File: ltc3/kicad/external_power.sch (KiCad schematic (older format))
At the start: 40 parts, among them IC701 TLP3542, IC702 TLP3542, IC703 TLP3542, IC704 TLP3542, M701 W28-XQ1A-1, M702 W28-XQ1A-1, M703 W28-XQ1A-1, M704 W28-XQ1A-1, P701 CONN_01X10, P702 CONN_01X10, P703 CONN_EXT_PWR_1, P704 CONN_EXT_PWR_2, P705 CONN_01X08, P706 CONN_01X08, P707 CONN_EXT_PWR_3, P708 CONN_EXT_PWR_4, Q701 PMV45EN, Q702 PMV45EN, Q703 PMV45EN, Q704 PMV45EN, SW701 SP3T, SW702 SP3T, SW703 SP3T, SW704 SP3T

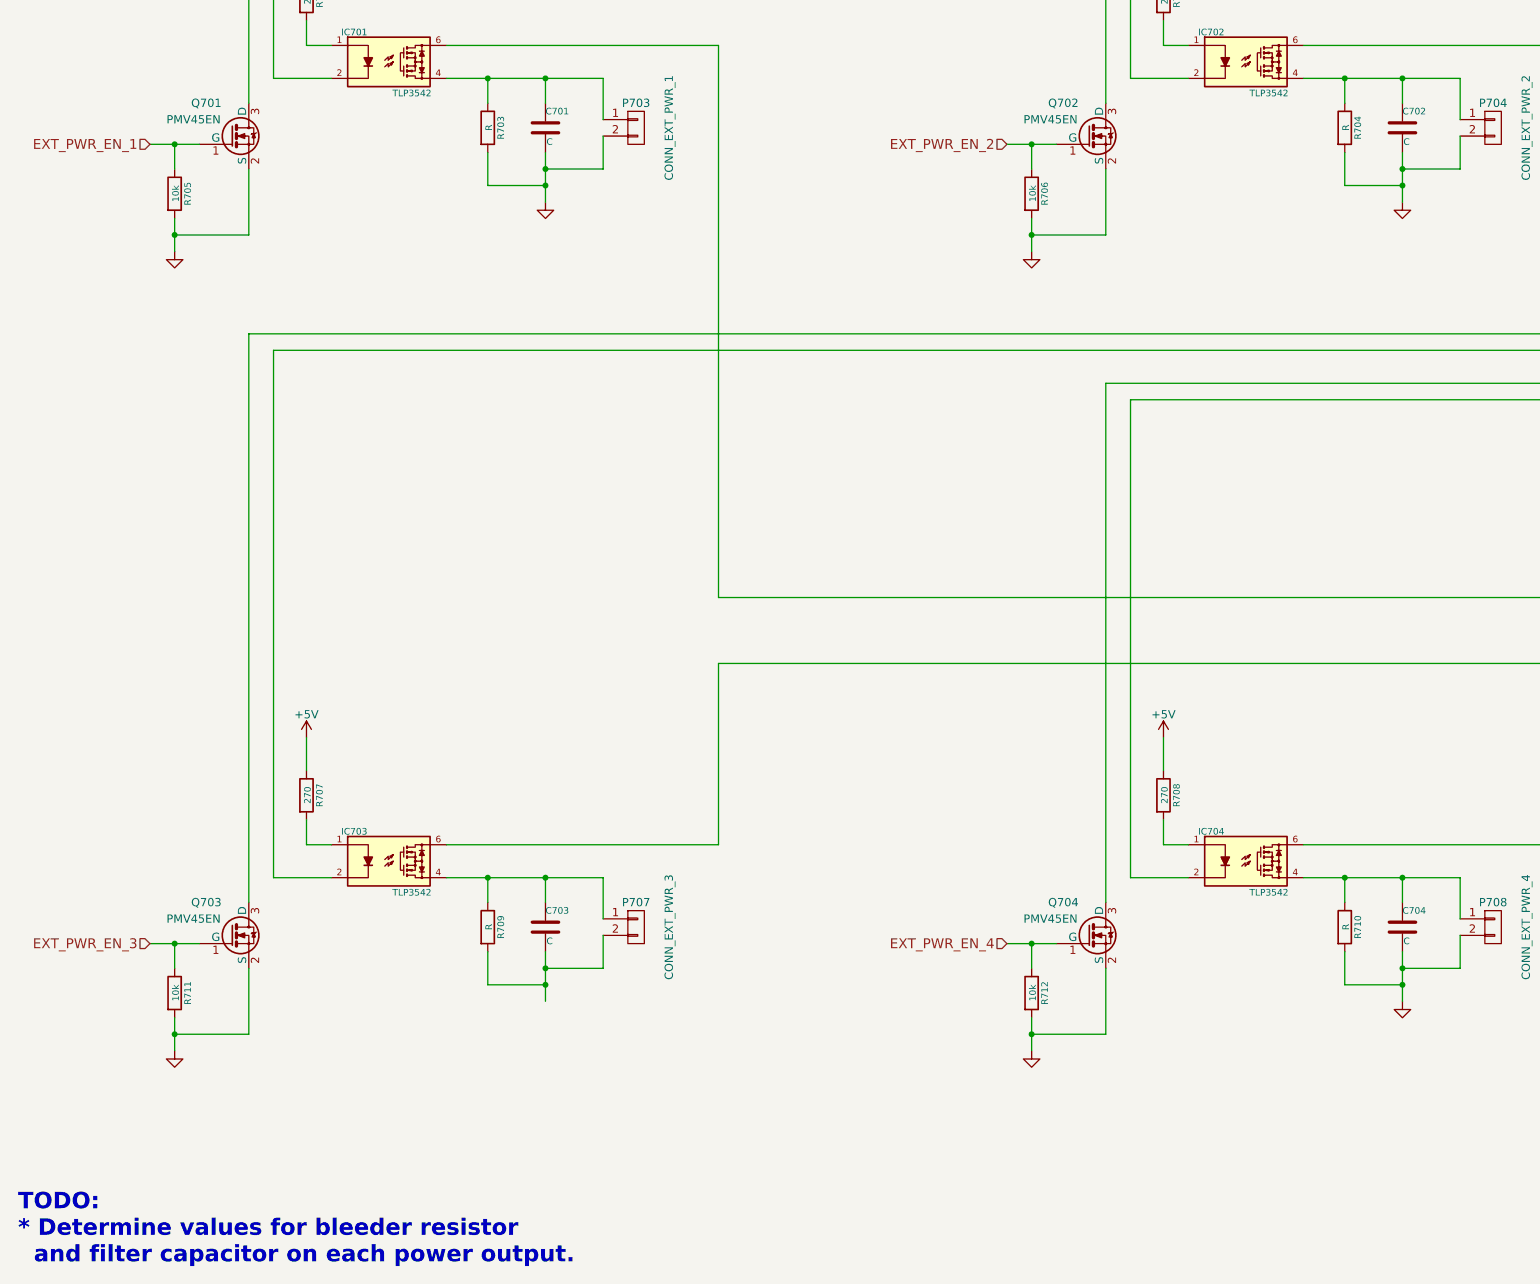
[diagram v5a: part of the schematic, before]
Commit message: LTC3: More component values and footprint assignments.
Split the two-in-one Beagle Bone expansion header component into two
separate components.  Otherwise, we'd be stuck with having to use a
single footprint for the BB cape pin headers, which means pin
numbering that doesn't match the BB docs.
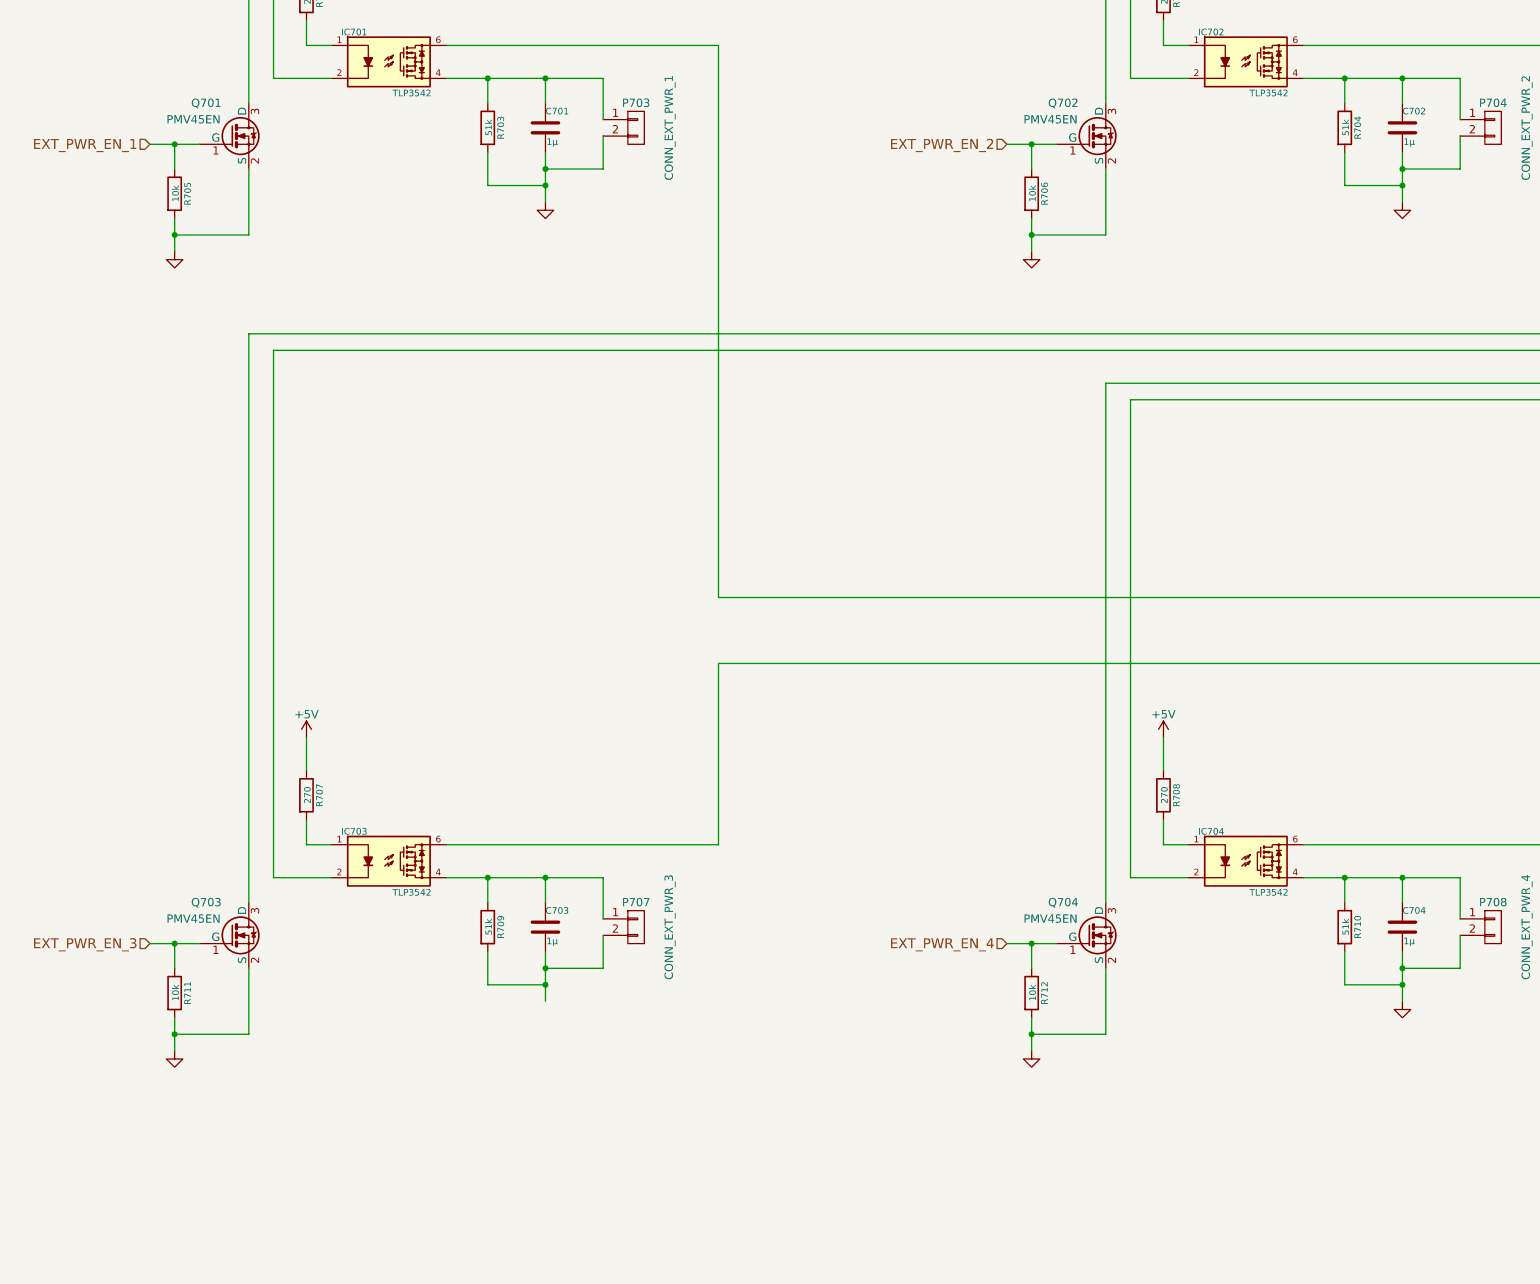
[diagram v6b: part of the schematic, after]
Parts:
- C701, C702, C703, C704: value C -> 1μ
- R703, R704, R709, R710: value R -> 51k
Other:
- note removed: "TODO:\n* Determine values for bleeder resistor\n and filter capacitor on each power output."
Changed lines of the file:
@@
 EESchema Schematic File Version 2
+LIBS:Launch_Tower_Computer_III-rescue
 LIBS:BeagleBone_Black
 LIBS:LT8490
@@
 LIBS:battery_single_cell
 LIBS:breakers
-LIBS:Launch_Tower_Computer_III-cache
 EELAYER 25 0
 EELAYER END
@@
 Comment4 ""
 $EndDescr
-Text Notes 700  10250 0    100  ~ 20
-TODO:\n* Determine values for bleeder resistor\n  and filter capacitor on each power output.
 $Comp
 L R R705
@@
 EXT_PWR_EN_1
 $Comp
-L GND #PWR0160
+L GND #PWR0161
 U 1 1 557E02AD
 P 1650 4100
-F 0 "#PWR0160" H 1650 4100 30  0001 C CNN
+F 0 "#PWR0161" H 1650 4100 30  0001 C CNN
 F 1 "GND" H 1650 4030 30  0001 C CNN
 F 2 "" H 1650 4100 60  0000 C CNN
@@
 P 3550 3350
 F 0 "R703" V 3630 3350 40  0000 C CNN
-F 1 "R" V 3557 3351 40  0000 C CNN
+F 1 "51k" V 3557 3351 40  0000 C CNN
 F 2 "" V 3480 3350 30  0001 C CNN
 F 3 "~" H 3550 3350 30  0000 C CNN
@@
 P 3900 3350
 F 0 "C701" H 3900 3450 40  0000 L CNN
-F 1 "C" H 3906 3265 40  0000 L CNN
+F 1 "1μ" H 3906 3265 40  0000 L CNN
 F 2 "" H 3938 3200 30  0001 C CNN
 F 3 "~" H 3900 3350 60  0000 C CNN
@@
 $EndComp
 $Comp
-L GND #PWR0161
+L GND #PWR0162
 U 1 1 557E02DD
 P 3900 3800
-F 0 "#PWR0161" H 3900 3800 30  0001 C CNN
+F 0 "#PWR0162" H 3900 3800 30  0001 C CNN
 F 1 "GND" H 3900 3730 30  0001 C CNN
 F 2 "" H 3900 3800 60  0000 C CNN
@@
 $EndComp
 $Comp
-L +5V #PWR0162
+L +5V #PWR0163
 U 1 1 56544A2B
 P 2450 2200
-F 0 "#PWR0162" H 2450 2050 50  0001 C CNN
+F 0 "#PWR0163" H 2450 2050 50  0001 C CNN
 F 1 "+5V" H 2450 2340 50  0000 C CNN
 F 2 "" H 2450 2200 60  0000 C CNN
@@
 EXT_PWR_EN_2
 $Comp
-L GND #PWR0163
+L GND #PWR0164
 U 1 1 56CA75BB
 P 6850 4100
-F 0 "#PWR0163" H 6850 4100 30  0001 C CNN
+F 0 "#PWR0164" H 6850 4100 30  0001 C CNN
 F 1 "GND" H 6850 4030 30  0001 C CNN
 F 2 "" H 6850 4100 60  0000 C CNN
@@
 P 8750 3350
 F 0 "R704" V 8830 3350 40  0000 C CNN
-F 1 "R" V 8757 3351 40  0000 C CNN
+F 1 "51k" V 8757 3351 40  0000 C CNN
 F 2 "" V 8680 3350 30  0001 C CNN
 F 3 "~" H 8750 3350 30  0000 C CNN
@@
 P 9100 3350
 F 0 "C702" H 9100 3450 40  0000 L CNN
-F 1 "C" H 9106 3265 40  0000 L CNN
+F 1 "1μ" H 9106 3265 40  0000 L CNN
 F 2 "Capacitors_SMD:C_0805" H 9138 3200 30  0001 C CNN
 F 3 "~" H 9100 3350 60  0000 C CNN
@@
 $EndComp
 $Comp
-L GND #PWR0164
+L GND #PWR0165
 U 1 1 56CA75CD
 P 9100 3800
-F 0 "#PWR0164" H 9100 3800 30  0001 C CNN
+F 0 "#PWR0165" H 9100 3800 30  0001 C CNN
 F 1 "GND" H 9100 3730 30  0001 C CNN
 F 2 "" H 9100 3800 60  0000 C CNN
@@
 $EndComp
 $Comp
-L +5V #PWR0165
+L +5V #PWR0166
 U 1 1 56CA760C
 P 7650 2200
-F 0 "#PWR0165" H 7650 2050 50  0001 C CNN
+F 0 "#PWR0166" H 7650 2050 50  0001 C CNN
 F 1 "+5V" H 7650 2340 50  0000 C CNN
 F 2 "" H 7650 2200 60  0000 C CNN
@@
 $EndComp
 $Comp
-L +12V #PWR0166
+L +12V #PWR0167
 U 1 1 56CA7612
 P 11800 5650
-F 0 "#PWR0166" H 11800 5500 50  0001 C CNN
+F 0 "#PWR0167" H 11800 5500 50  0001 C CNN
 F 1 "+12V" H 11800 5790 50  0000 C CNN
 F 2 "" H 11800 5650 60  0000 C CNN
@@
 EXT_PWR_EN_3
 $Comp
-L GND #PWR0167
+L GND #PWR0168
 U 1 1 56CA9336
 P 1650 8950
-F 0 "#PWR0167" H 1650 8950 30  0001 C CNN
+F 0 "#PWR0168" H 1650 8950 30  0001 C CNN
 F 1 "GND" H 1650 8880 30  0001 C CNN
 F 2 "" H 1650 8950 60  0000 C CNN
@@
 P 3550 8200
 F 0 "R709" V 3630 8200 40  0000 C CNN
-F 1 "R" V 3557 8201 40  0000 C CNN
+F 1 "51k" V 3557 8201 40  0000 C CNN
 F 2 "" V 3480 8200 30  0001 C CNN
 F 3 "~" H 3550 8200 30  0000 C CNN
@@
 P 3900 8200
 F 0 "C703" H 3900 8300 40  0000 L CNN
-F 1 "C" H 3906 8115 40  0000 L CNN
+F 1 "1μ" H 3906 8115 40  0000 L CNN
 F 2 "Capacitors_SMD:C_0805" H 3938 8050 30  0001 C CNN
 F 3 "~" H 3900 8200 60  0000 C CNN
@@
 $EndComp
 $Comp
-L +5V #PWR0168
+L +5V #PWR0169
 U 1 1 56CA9387
 P 2450 7050
-F 0 "#PWR0168" H 2450 6900 50  0001 C CNN
+F 0 "#PWR0169" H 2450 6900 50  0001 C CNN
 F 1 "+5V" H 2450 7190 50  0000 C CNN
 F 2 "" H 2450 7050 60  0000 C CNN
@@
 EXT_PWR_EN_4
 $Comp
-L GND #PWR0169
+L GND #PWR0170
 U 1 1 56CA93AD
 P 6850 8950
-F 0 "#PWR0169" H 6850 8950 30  0001 C CNN
+F 0 "#PWR0170" H 6850 8950 30  0001 C CNN
 F 1 "GND" H 6850 8880 30  0001 C CNN
 F 2 "" H 6850 8950 60  0000 C CNN
@@
 P 8750 8200
 F 0 "R710" V 8830 8200 40  0000 C CNN
-F 1 "R" V 8757 8201 40  0000 C CNN
+F 1 "51k" V 8757 8201 40  0000 C CNN
 F 2 "" V 8680 8200 30  0001 C CNN
 F 3 "~" H 8750 8200 30  0000 C CNN
@@
 P 9100 8200
 F 0 "C704" H 9100 8300 40  0000 L CNN
-F 1 "C" H 9106 8115 40  0000 L CNN
+F 1 "1μ" H 9106 8115 40  0000 L CNN
 F 2 "Capacitors_SMD:C_0805" H 9138 8050 30  0001 C CNN
 F 3 "~" H 9100 8200 60  0000 C CNN
@@
 $EndComp
 $Comp
-L GND #PWR0170
+L GND #PWR0171
 U 1 1 56CA93BF
 P 9100 8650
-F 0 "#PWR0170" H 9100 8650 30  0001 C CNN
+F 0 "#PWR0171" H 9100 8650 30  0001 C CNN
 F 1 "GND" H 9100 8580 30  0001 C CNN
 F 2 "" H 9100 8650 60  0000 C CNN
@@
 $EndComp
 $Comp
-L +5V #PWR0171
+L +5V #PWR0172
 U 1 1 56CA93FE
 P 7650 7050
-F 0 "#PWR0171" H 7650 6900 50  0001 C CNN
+F 0 "#PWR0172" H 7650 6900 50  0001 C CNN
 F 1 "+5V" H 7650 7190 50  0000 C CNN
 F 2 "" H 7650 7050 60  0000 C CNN
@@
 Manual Override Switches, Front Panel
 $Comp
-L GND #PWR0172
+L GND #PWR0173
 U 1 1 56DB5084
 P 11800 2800
-F 0 "#PWR0172" H 11800 2550 50  0001 C CNN
+F 0 "#PWR0173" H 11800 2550 50  0001 C CNN
 F 1 "GND" H 11808 2626 50  0001 C CNN
 F 2 "" H 11800 2800 50  0000 C CNN

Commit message: Assigned component footprints.
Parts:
- C701: footprint (none) -> Capacitors_SMD:C_0805
- R703, R704, R709, R710: footprint (none) -> Resistors_SMD:R_0805
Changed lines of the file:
@@
 EESchema Schematic File Version 2
-LIBS:Launch_Tower_Computer_III-rescue
 LIBS:BeagleBone_Black
 LIBS:LT8490
@@
 LIBS:battery_single_cell
 LIBS:breakers
+LIBS:Launch_Tower_Computer_III-cache
 EELAYER 25 0
 EELAYER END
@@
 F 0 "R703" V 3630 3350 40  0000 C CNN
 F 1 "51k" V 3557 3351 40  0000 C CNN
-F 2 "" V 3480 3350 30  0001 C CNN
+F 2 "Resistors_SMD:R_0805" V 3480 3350 30  0001 C CNN
 F 3 "~" H 3550 3350 30  0000 C CNN
 	1    3550 3350
@@
 F 0 "C701" H 3900 3450 40  0000 L CNN
 F 1 "1μ" H 3906 3265 40  0000 L CNN
-F 2 "" H 3938 3200 30  0001 C CNN
+F 2 "Capacitors_SMD:C_0805" H 3938 3200 30  0001 C CNN
 F 3 "~" H 3900 3350 60  0000 C CNN
 	1    3900 3350
@@
 F 0 "R704" V 8830 3350 40  0000 C CNN
 F 1 "51k" V 8757 3351 40  0000 C CNN
-F 2 "" V 8680 3350 30  0001 C CNN
+F 2 "Resistors_SMD:R_0805" V 8680 3350 30  0001 C CNN
 F 3 "~" H 8750 3350 30  0000 C CNN
 	1    8750 3350
@@
 F 0 "R709" V 3630 8200 40  0000 C CNN
 F 1 "51k" V 3557 8201 40  0000 C CNN
-F 2 "" V 3480 8200 30  0001 C CNN
+F 2 "Resistors_SMD:R_0805" V 3480 8200 30  0001 C CNN
 F 3 "~" H 3550 8200 30  0000 C CNN
 	1    3550 8200
@@
 F 0 "R710" V 8830 8200 40  0000 C CNN
 F 1 "51k" V 8757 8201 40  0000 C CNN
-F 2 "" V 8680 8200 30  0001 C CNN
+F 2 "Resistors_SMD:R_0805" V 8680 8200 30  0001 C CNN
 F 3 "~" H 8750 8200 30  0000 C CNN
 	1    8750 8200
